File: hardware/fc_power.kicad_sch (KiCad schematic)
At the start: 30 parts, among them U12 LP5912-1.8DRVR, U3 LMR51430YFDDCR, U4 LMR51430YFDDCR, U7 LP5912-3.3DRVR

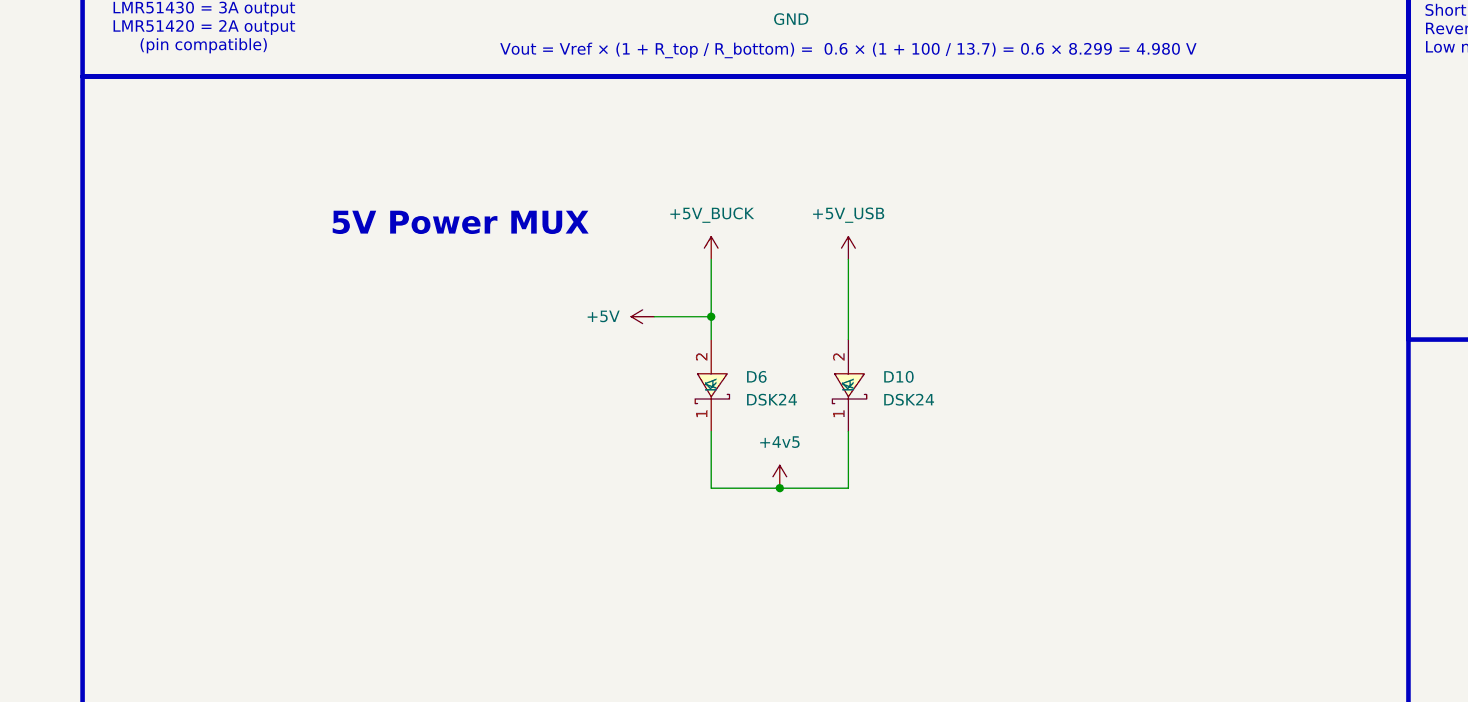
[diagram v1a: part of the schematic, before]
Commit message: Drop the ESC sheets again; CSA taken into fc_power
esc_4in1 and ESC removed from the root and the tree. fc_power carries
Stan's in-progress edits with the current-sense parts.
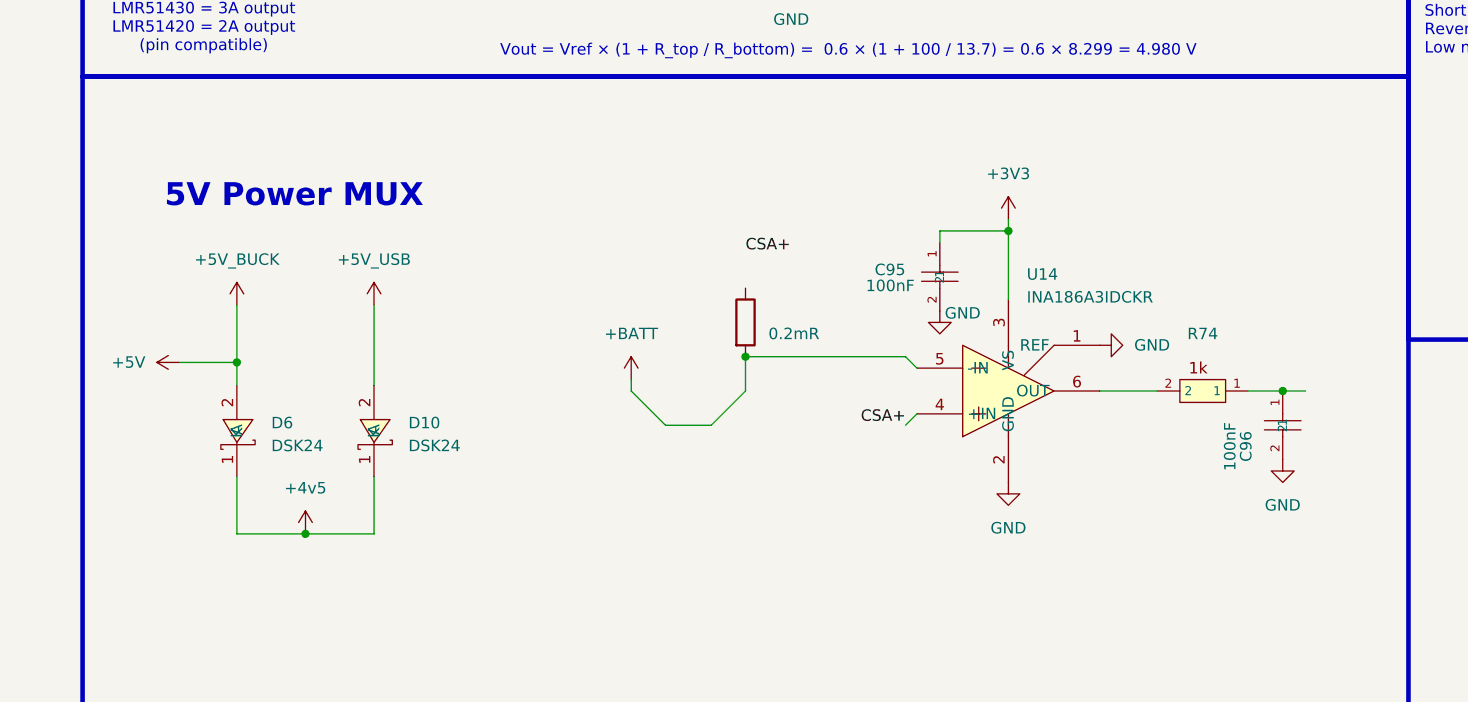
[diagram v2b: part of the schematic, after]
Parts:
- added C95, C96: 100nF, Capacitor_SMD:C_0201_0603Metric, symbol ESCLibrary:GRM033R61C104KE84D
- added R74: 1k, 4in1ESC:R_0201_0603Metric, symbol ESCLibrary:0201_1kR
- added Rsense2: 0.2mR, Resistor_SMD:R_2512_6332Metric, symbol Device:R
- added U14: INA186A3IDCKR, 4in1ESC:SOT-363_SC-70-6, symbol components:INA186A3IDCKR
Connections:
- net +BATT: now also Rsense2.2, U14.5 (-IN)
- net GND: now also C95.2, C96.2, U14.1 (REF), U14.2 (GND)
- new net: C96.1, R74.1
- new net: R74.2, U14.6 (OUT)
- new net +3V3: C95.1, U14.3 (VS)
- new net CSA+: U14.4 (+IN)
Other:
- moved on the sheet: D10, D6

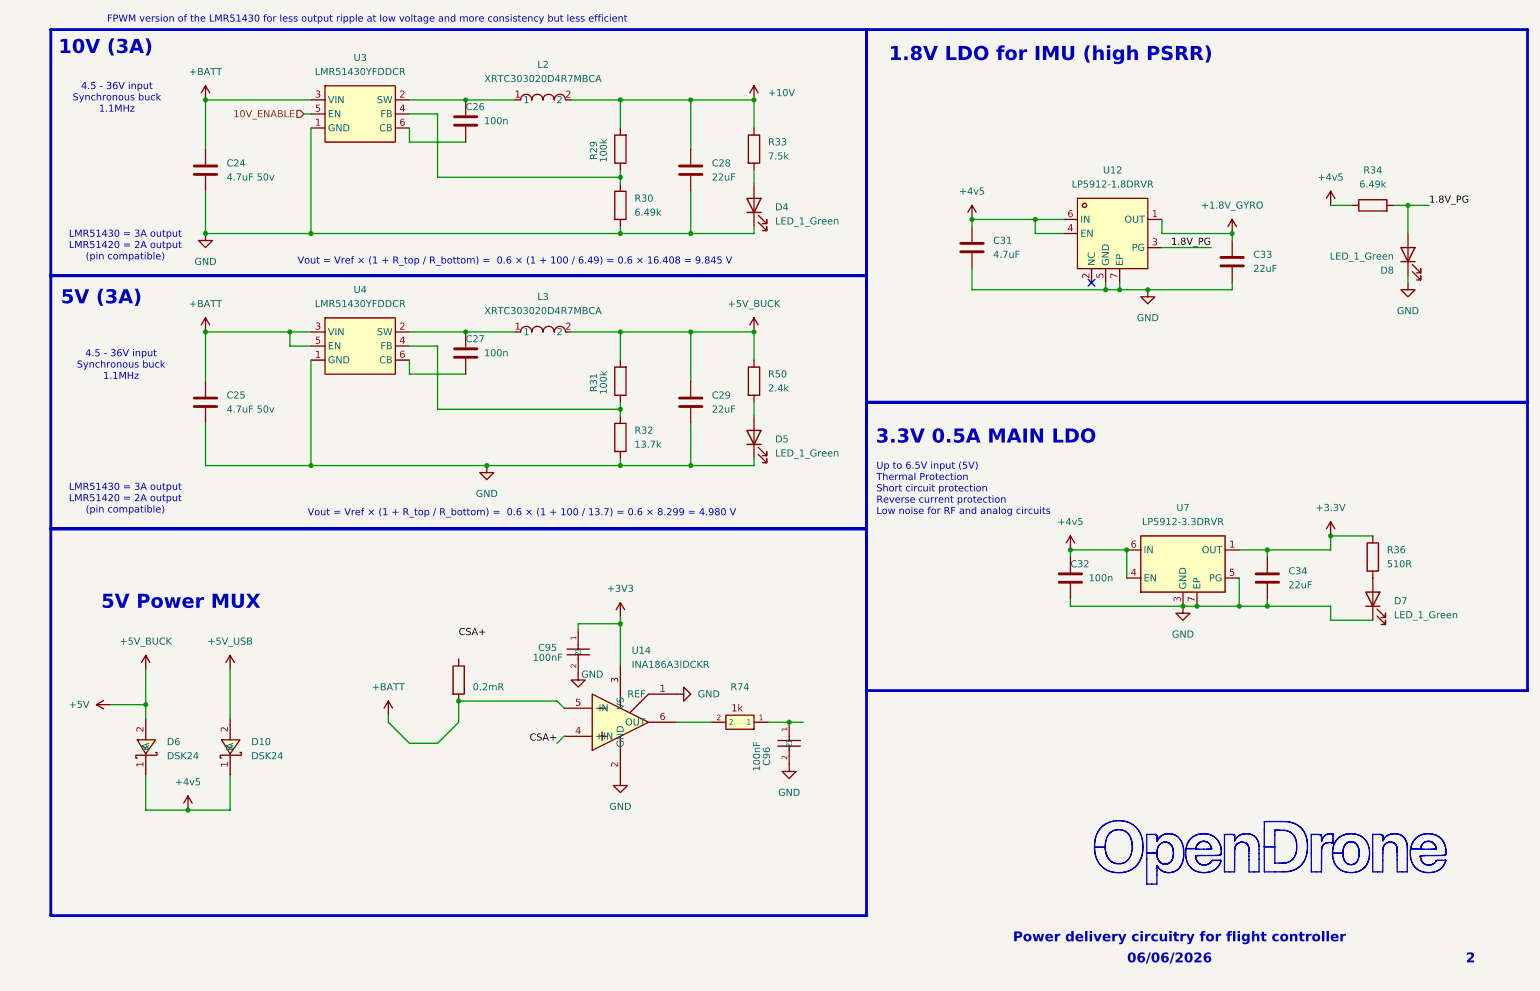
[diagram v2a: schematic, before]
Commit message: Net classes: VBAT, Phase, Power, Gate, USB, RF, Analog with colours and patterns
Replaces the stale 50Ohm /ELRS/* patterns inherited from the template.
Widths and clearances start from the line standard (0.09/0.09, via 0.35/0.20)
and the ESC boards' practice; USB and RF geometry still to be checked against
the chosen JLCPCB 6-layer stackup.
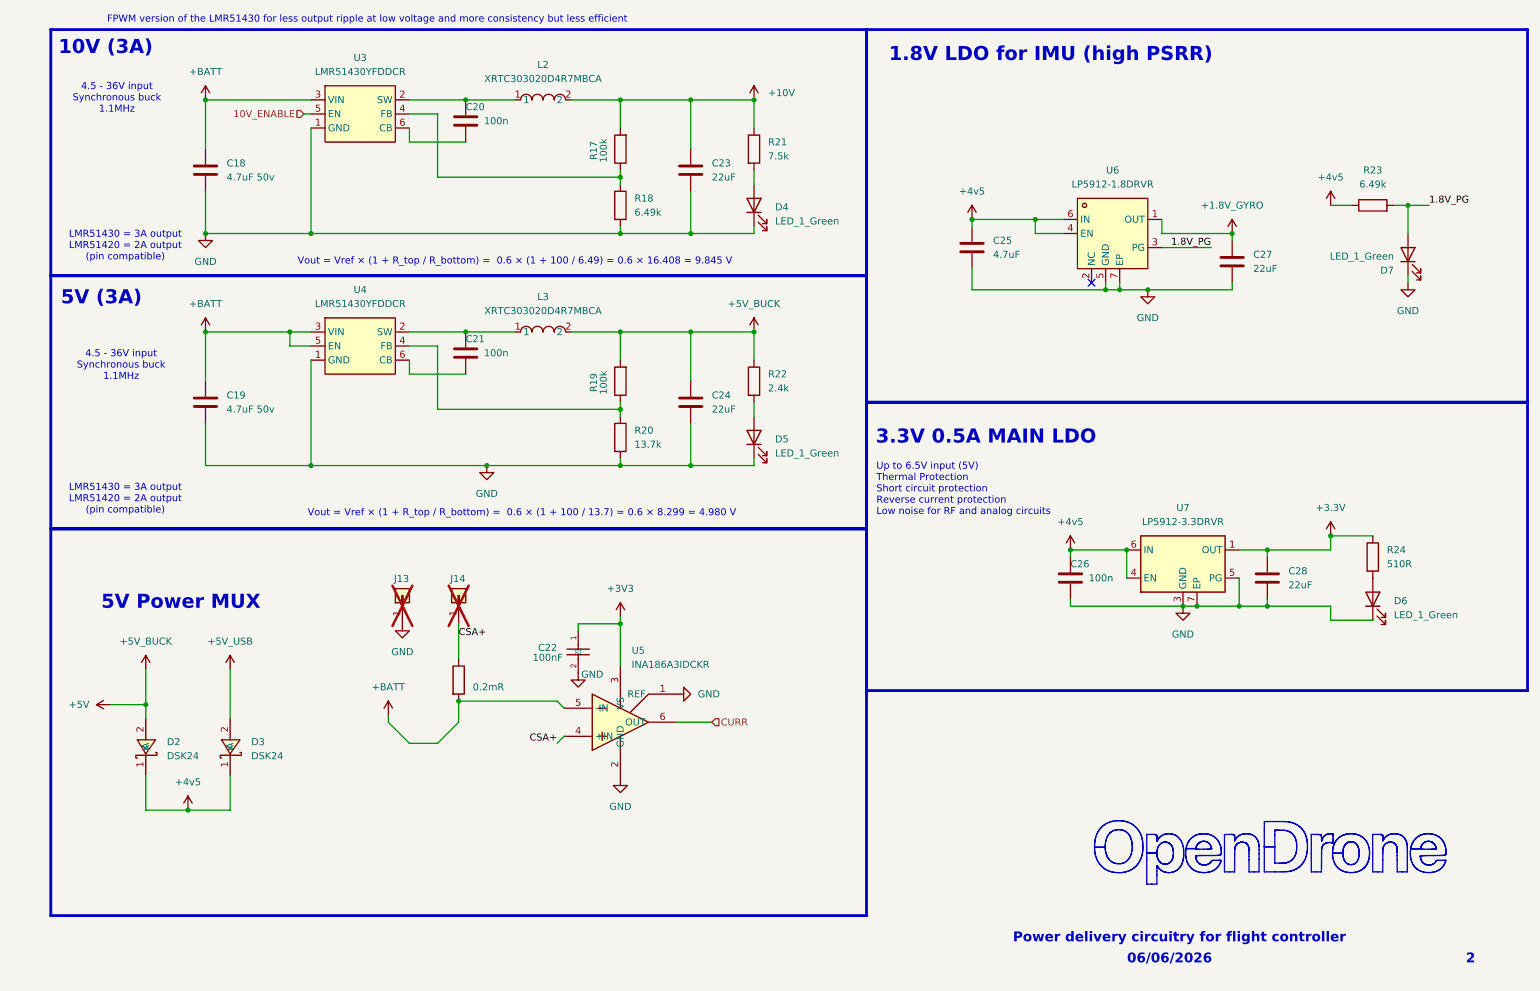
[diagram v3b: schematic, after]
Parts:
- removed C96: 100nF, Capacitor_SMD:C_0201_0603Metric, symbol ESCLibrary:GRM033R61C104KE84D
- removed R74: 1k, 4in1ESC:R_0201_0603Metric, symbol ESCLibrary:0201_1kR
- added J13, J14: 5V, lib:small_pad, symbol Connector_Generic:Conn_01x01
- renumbered C24 to C18, C25 to C19, C26 to C20, C27 to C21, C95 to C22, C28 to C23, C29 to C24, C31 to C25, C32 to C26, C33 to C27, C34 to C28, D6 to D2, D10 to D3, D7 to D6, D8 to D7, R29 to R17, R30 to R18, R31 to R19, R32 to R20, R33 to R21, R50 to R22, R34 to R23, R36 to R24, Rsense2 to Rsense1, U14 to U5, U12 to U6
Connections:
- net CSA+: now also Rsense1.1, J14.1 (Pin_1)
- net GND: now also J13.1 (Pin_1)
- net CURR: now reaches U5.6 (OUT)

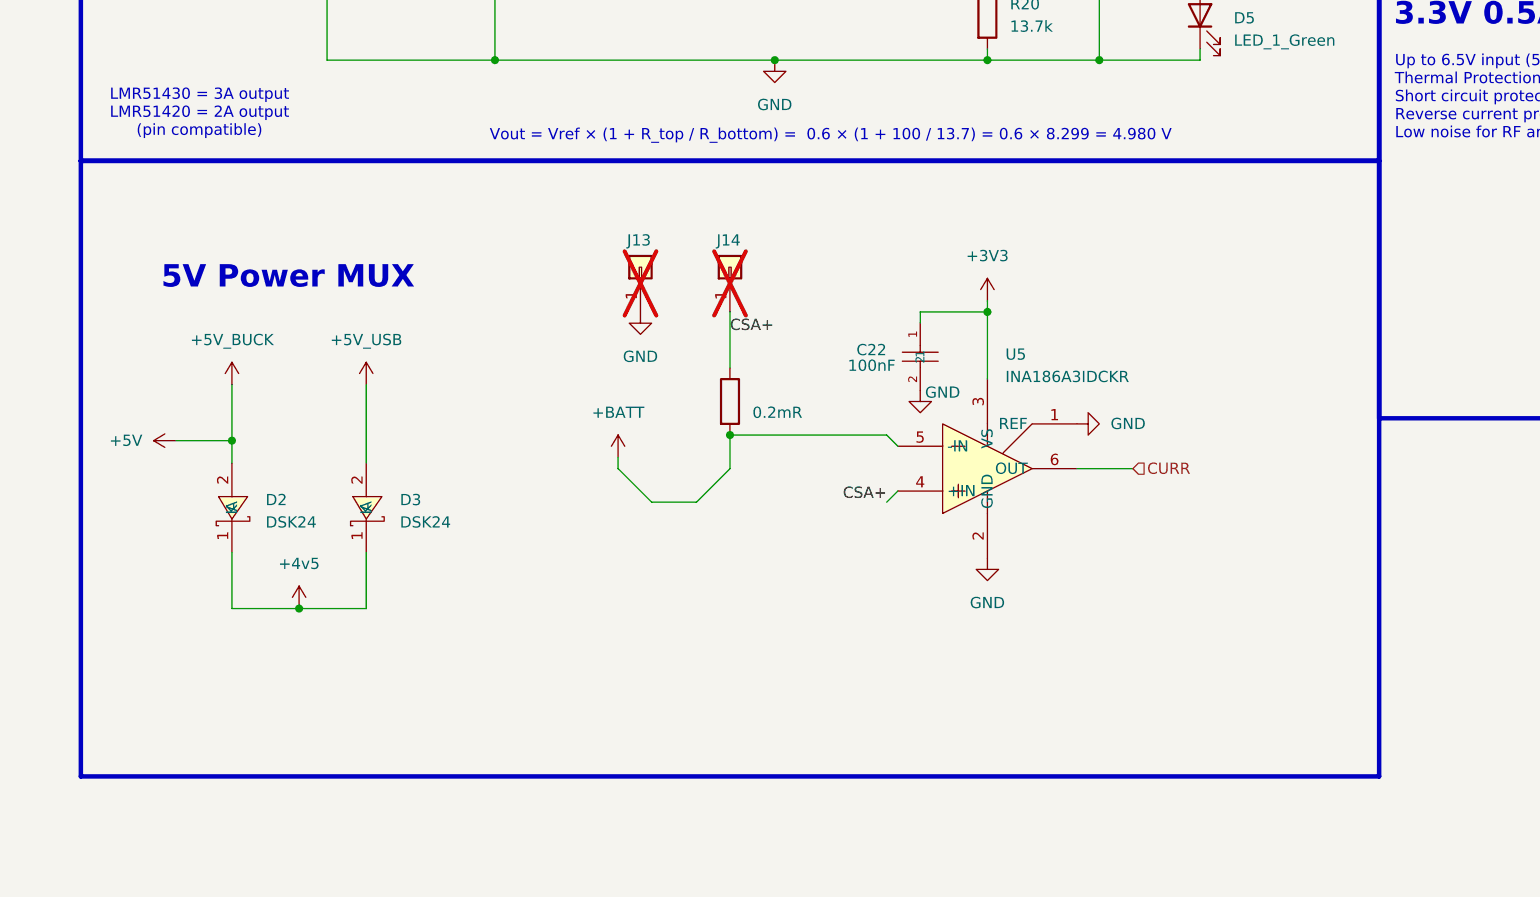
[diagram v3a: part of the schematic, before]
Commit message: OpenAIO: master PCB with Base and Core islands routed, AIO_outline footprint+symbol in project lib
Save point before the two-board (LGA) split tooling.
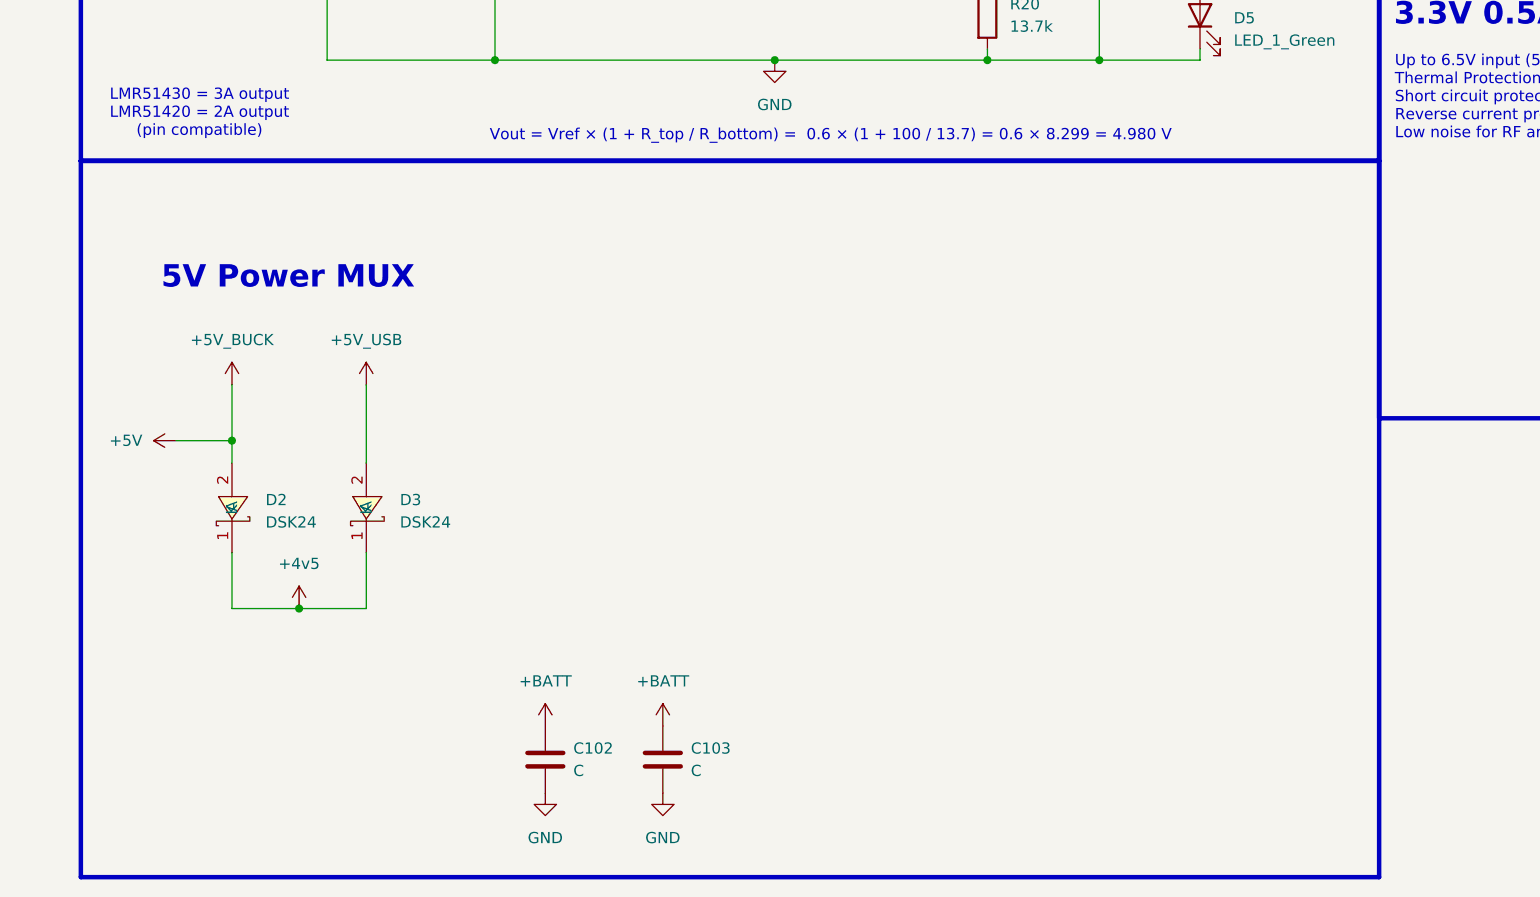
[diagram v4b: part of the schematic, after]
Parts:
- removed C22: 100nF, Capacitor_SMD:C_0201_0603Metric, symbol ESCLibrary:GRM033R61C104KE84D
- removed J13, J14: 5V, lib:small_pad, symbol Connector_Generic:Conn_01x01
- removed Rsense1: 0.2mR, Resistor_SMD:R_2512_6332Metric, symbol Device:R
- removed U5: INA186A3IDCKR, 4in1ESC:SOT-363_SC-70-6, symbol components:INA186A3IDCKR
- added C102, C103: C, Capacitor_SMD:C_0805_2012Metric, symbol Device:C
- C18, C19, C20, C21, C23, C24, C25, C26, C27, C28, D4, D5, D6, D7, R17, R18, R19, R20, R21, R22, R23, R24: KiLib_Generator (none) -> SMD_2terminal_chip_molded
- D2, D3: LCSC Part (none) -> C64890
- U6, U7: KiLib_Generator (none) -> package/no_lead
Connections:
- net +BATT: now also C102.1, C103.1
- net GND: now also C102.2, C103.2

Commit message: OpenAIO: Core outline from User.2 to Edge.Cuts, J90/J91 re-placed with nets, Core rule area, derived boards refreshed
tools/core_outline.py moves the closed User.2 contour of the Core island to
Edge.Cuts. J90 sits in the free area of the Base top (78.9, 62.0), J91 inside
the Core outline (114.1, 53.55) on B.Cu; lga_place.py now assigns pad nets
from the pin table. Rule area Core redrawn from the new outline; split re-run,
J90 carries the new Core STEP and 23.1 x 20.2 mm shadow.
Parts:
- added C105, C106: C, Capacitor_SMD:C_1206_3216Metric, symbol Device:C
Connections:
- net +BATT: now also C105.1, C106.1
- net GND: now also C105.2, C106.2
